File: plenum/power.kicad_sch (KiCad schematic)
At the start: 43 parts, among them U16 TPS62082, U17 TPS54294

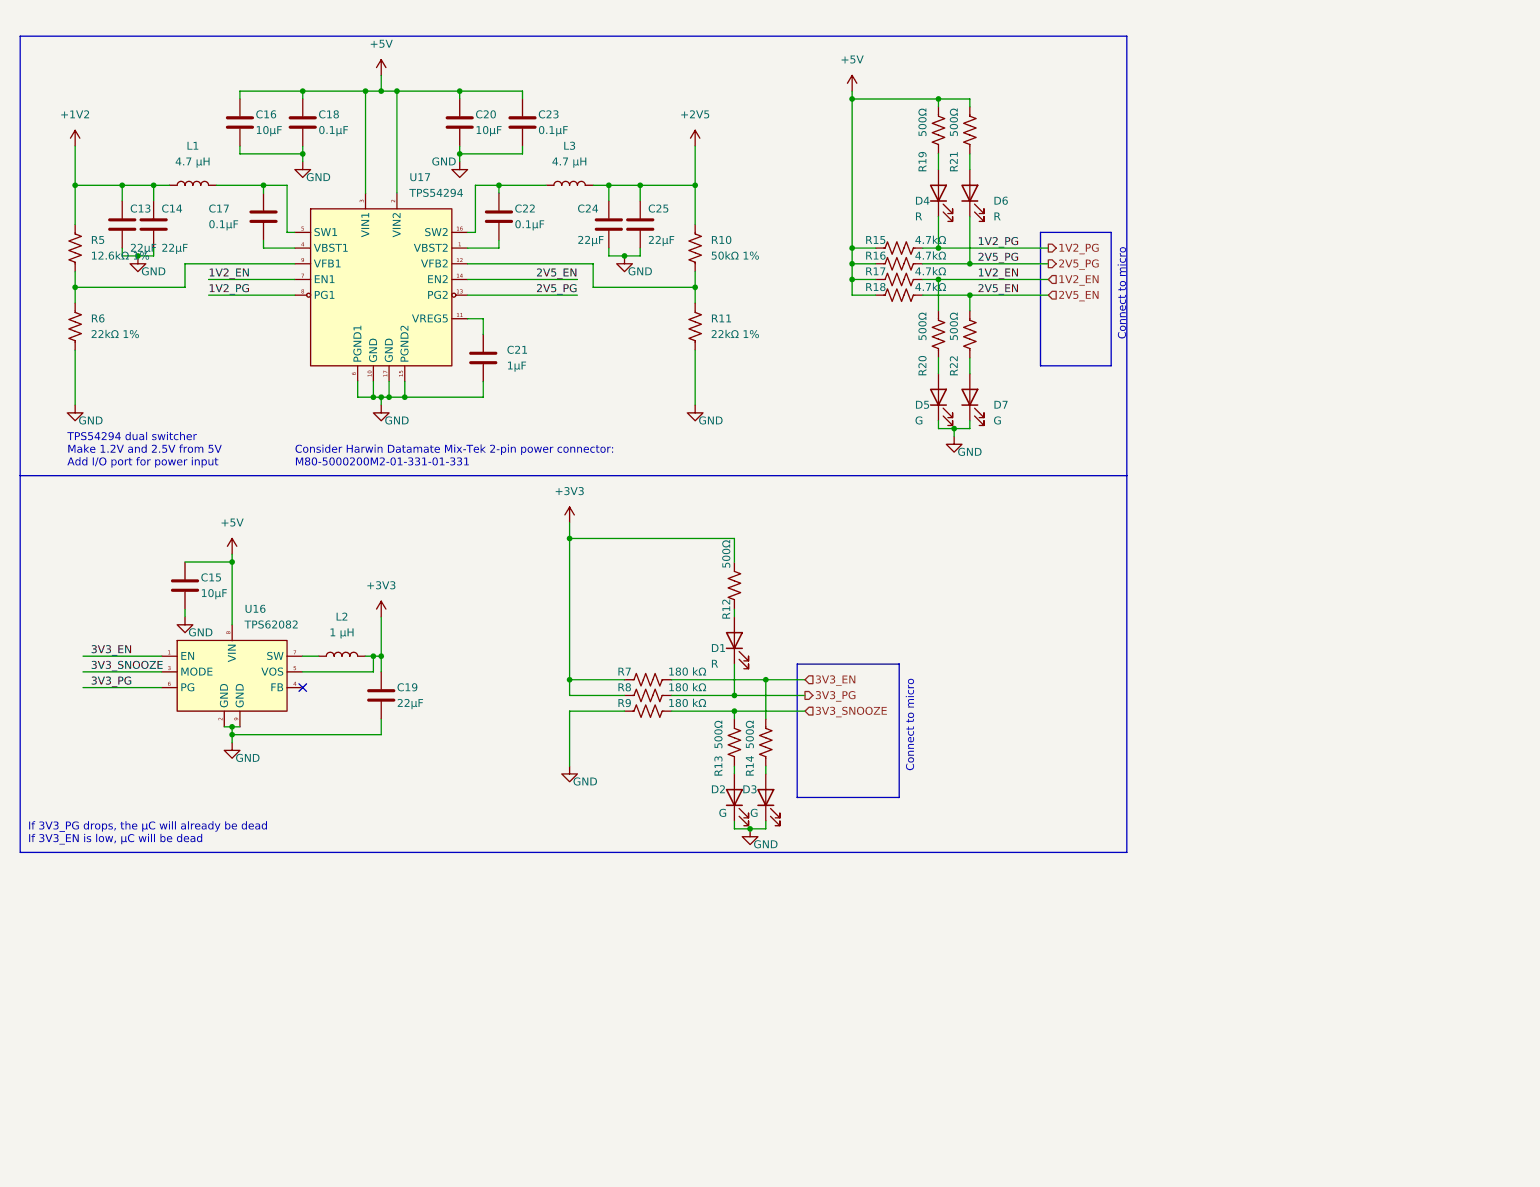
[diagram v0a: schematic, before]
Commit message: adding housekeeping board
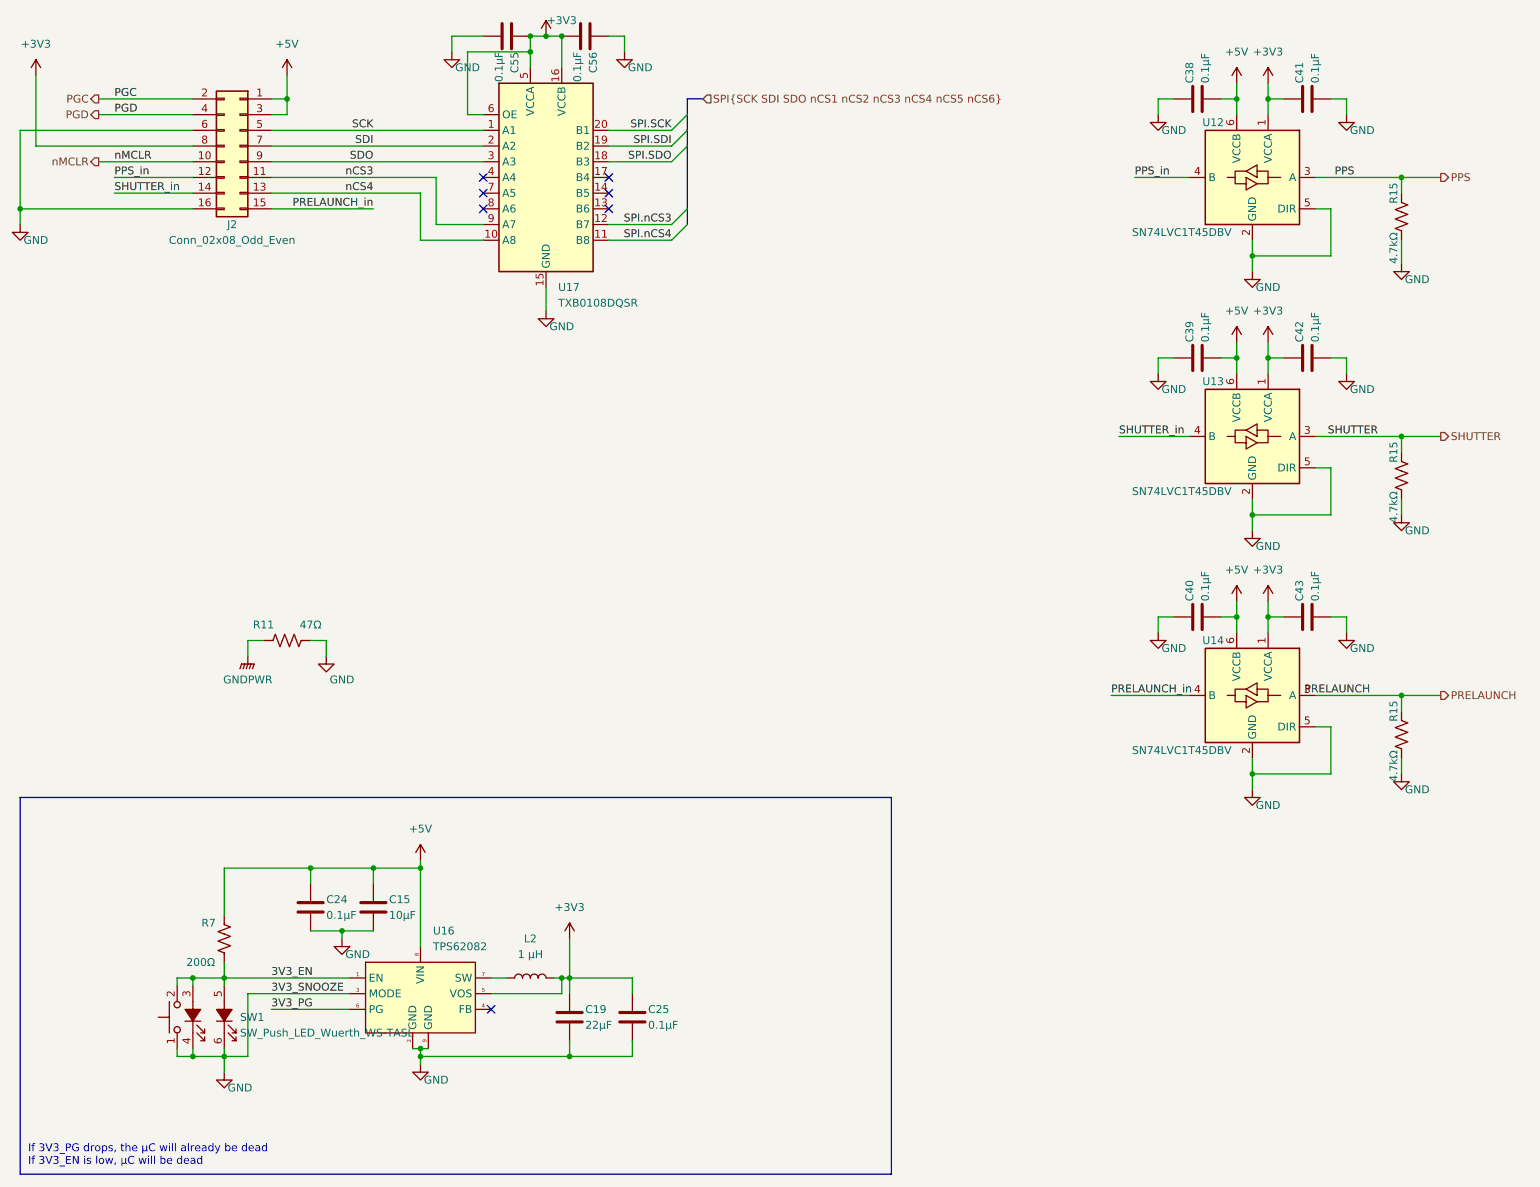
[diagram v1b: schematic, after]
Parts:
- removed C13, C14: 22µF, Capacitor_SMD:C_1206_3216Metric, symbol Device:C
- removed C16, C20: 10µF, Capacitor_SMD:C_0805_2012Metric, symbol Device:C
- removed C17, C18, C22, C23: 0.1µF, Capacitor_SMD:C_0402_1005Metric, symbol Device:C
- removed C21: 1µF, Capacitor_SMD:C_0603_1608Metric, symbol Device:C
- removed D1, D6: R, symbol Device:LED
- removed D2, D3, D5, D7: G, symbol Device:LED
- removed D4: R, Capacitor_SMD:C_0402_1005Metric, symbol Device:LED
- removed L1, L3: 4.7 µH, Inductor_SMD:L_Wuerth_MAPI-4030, symbol Device:L
- removed R10: 50kΩ 1%, Resistor_SMD:R_0603_1608Metric, symbol Device:R_US
- removed R12, R13, R14, R19, R20, R21, R22: 500Ω, Resistor_SMD:R_0603_1608Metric, symbol Device:R_US
- removed R15, R16, R17, R18: 4.7kΩ, Resistor_SMD:R_0603_1608Metric, symbol Device:R_US
- removed R5: 12.6kΩ 1%, Resistor_SMD:R_0603_1608Metric, symbol Device:R_US
- removed R6: 22kΩ 1%, Resistor_SMD:R_0603_1608Metric, symbol Device:R_US
- removed R8, R9: 180 kΩ, Resistor_SMD:R_0603_1608Metric, symbol Device:R_US
- removed U17: TPS54294, Package_DFN_QFN:Texas_S-PVQFN-N16_EP2.7x2.7mm, symbol Regulator_Switching:TPS54294
- added C38, C39, C40, C41, C42, C43, C55, C56: 0.1µF, Capacitor_SMD:C_0603_1608Metric, symbol Device:C
- added J2: Conn_02x08_Odd_Even, Connector_PinHeader_2.54mm:PinHeader_2x08_P2.54mm_Vertical, symbol Connector_Generic:Conn_02x08_Odd_Even
- added R15 (x3): 4.7kΩ, Resistor_SMD:R_0603_1608Metric, symbol Device:R_US
- added SW1: SW_Push_LED_Wuerth_WS-TASL, Button_Switch_SMD:SW_Tactile_SPST_Wuerth_WS-TASL, symbol Switch:SW_Push_LED_Wuerth_WS-TASL
- added U12, U13, U14: SN74LVC1T45DBV, Package_TO_SOT_SMD:SOT-23-6, symbol Logic_LevelTranslator:SN74LVC1T45DBV
- added U17: TXB0108DQSR, Package_SON:USON-20_2x4mm_P0.4mm, symbol Logic_LevelTranslator:TXB0108DQSR
- C15, C19: footprint Capacitor_SMD:C_0805_2012Metric -> Capacitor_SMD:C_1206_3216Metric
- C24, C25: value 22µF -> 0.1µF; footprint Capacitor_SMD:C_1206_3216Metric -> Capacitor_SMD:C_0603_1608Metric
- R11: value 22kΩ 1% -> 47Ω; footprint Resistor_SMD:R_0603_1608Metric -> Resistor_SMD:R_1210_3225Metric
- R7: value 180 kΩ -> 200Ω
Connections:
- net 3V3_SNOOZE is gone; now on net GND: U16.3 (MODE)
- net +3V3: now also C25.2, C41.2, C42.2, C43.2, C55.2, C56.1, J2.8 (Pin_8), U12.1 (VCCA), U13.1 (VCCA), U14.1 (VCCA), U17.16 (VCCB), U17.5 (VCCA), U17.6 (OE); no longer R7.2
- net +5V: now also C24.2, R7.2, C38.1, C39.1, C40.1, J2.1 (Pin_1), J2.3 (Pin_3), U12.6 (VCCB), U13.6 (VCCB), U14.6 (VCCB)
- net 3V3_EN: now also SW1.2 (sw2), SW1.3 (A), SW1.5 (A)
- net GND: now also C38.2, C39.2, C40.2, C41.1, C42.1, C43.1, C55.1, C56.2, J2.16 (Pin_16), J2.6 (Pin_6), R15.1, R15.1, R15.1, SW1.1 (sw1), SW1.4 (K), SW1.6 (K), U12.2 (GND), U12.5 (DIR), U13.2 (GND), U13.5 (DIR), U14.2 (GND), U14.5 (DIR), U17.15 (GND)
- net GNDPWR: now reaches R11.1
- removed net +2V5: C24.2, C25.2
- new net PGC: J2.2 (Pin_2)
- new net PGD: J2.4 (Pin_4)
- new net PPS: R15.2, U12.3 (A)
- new net PPS_in: J2.12 (Pin_12), U12.4 (B)
- new net PRELAUNCH: R15.2, U14.3 (A)
- new net PRELAUNCH_in: J2.15 (Pin_15), U14.4 (B)
- new net SCK: J2.5 (Pin_5), U17.1 (A1)
- new net SDI: J2.7 (Pin_7), U17.2 (A2)
- new net SDO: J2.9 (Pin_9), U17.3 (A3)
- new net SHUTTER: R15.2, U13.3 (A)
- new net SHUTTER_in: J2.14 (Pin_14), U13.4 (B)
- new net SPI.SCK: U17.20 (B1)
- new net SPI.SDI: U17.19 (B2)
- new net SPI.SDO: U17.18 (B3)
- new net SPI.nCS3: U17.12 (B7)
- new net SPI.nCS4: U17.11 (B8)
- new net nCS3: J2.11 (Pin_11), U17.9 (A7)
- new net nCS4: J2.13 (Pin_13), U17.10 (A8)
- new net nMCLR: J2.10 (Pin_10)
- no-connect marks 1 -> 7
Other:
- note removed: "Connect to micro"
- note removed: "Consider Harwin Datamate Mix-Tek 2-pin power connector: M80-5000200M2-01-331-01-331"
- note removed: "TPS54294 dual switcher Make 1.2V and 2.5V from 5V Add I/O port for power input"
- moved on the sheet: C15, C19, L2, U16
